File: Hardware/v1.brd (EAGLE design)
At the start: 50 x 40 mm, 83 parts, among them IC1 LM324D, IC2 m328p, IC3 REG1117, J2 22-27-2031-03, J3 22-27-2021-02, J4 22-27-2031-03, J5 22-27-2041-04, J6 22-27-2071-07, Q1 BSS123, Q2 BSS123, Q3 BSS123, Q5 BSS123

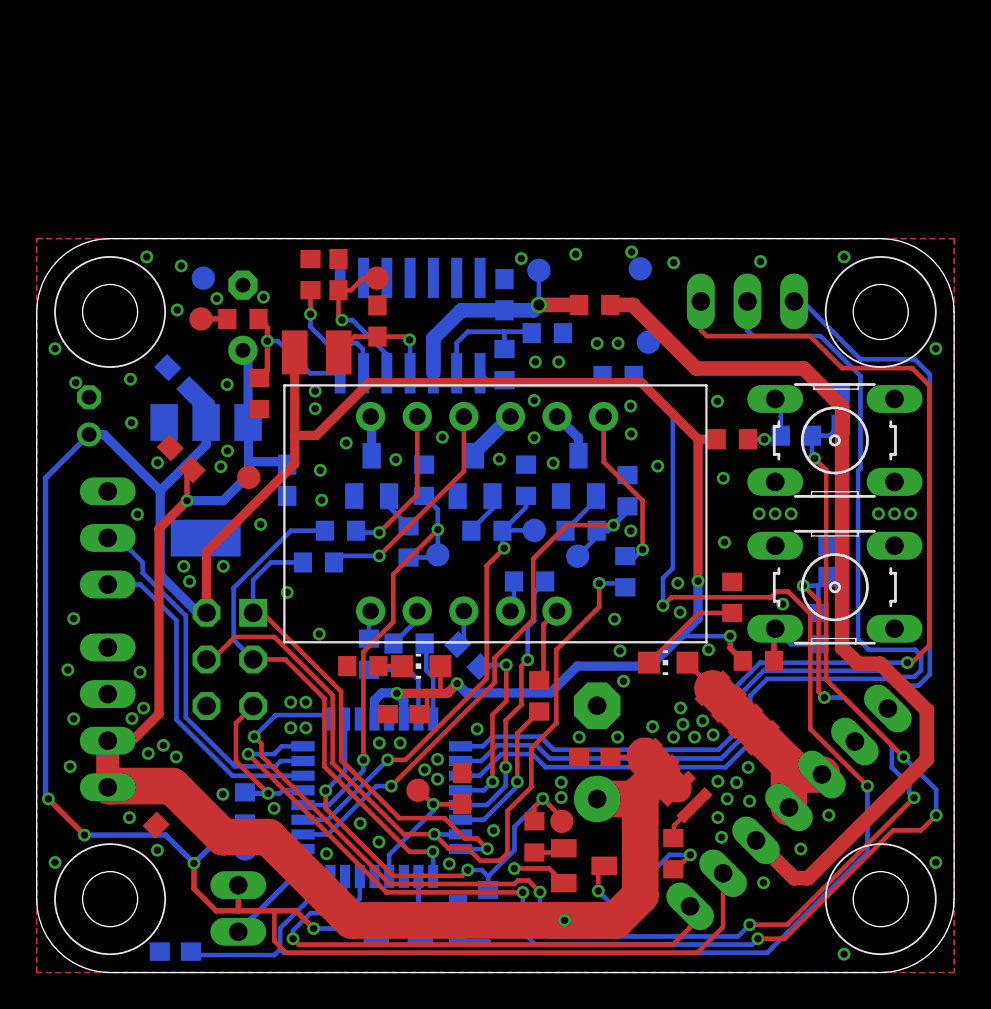
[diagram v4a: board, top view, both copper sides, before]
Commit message: all changes described in #64 pull ups are 10k
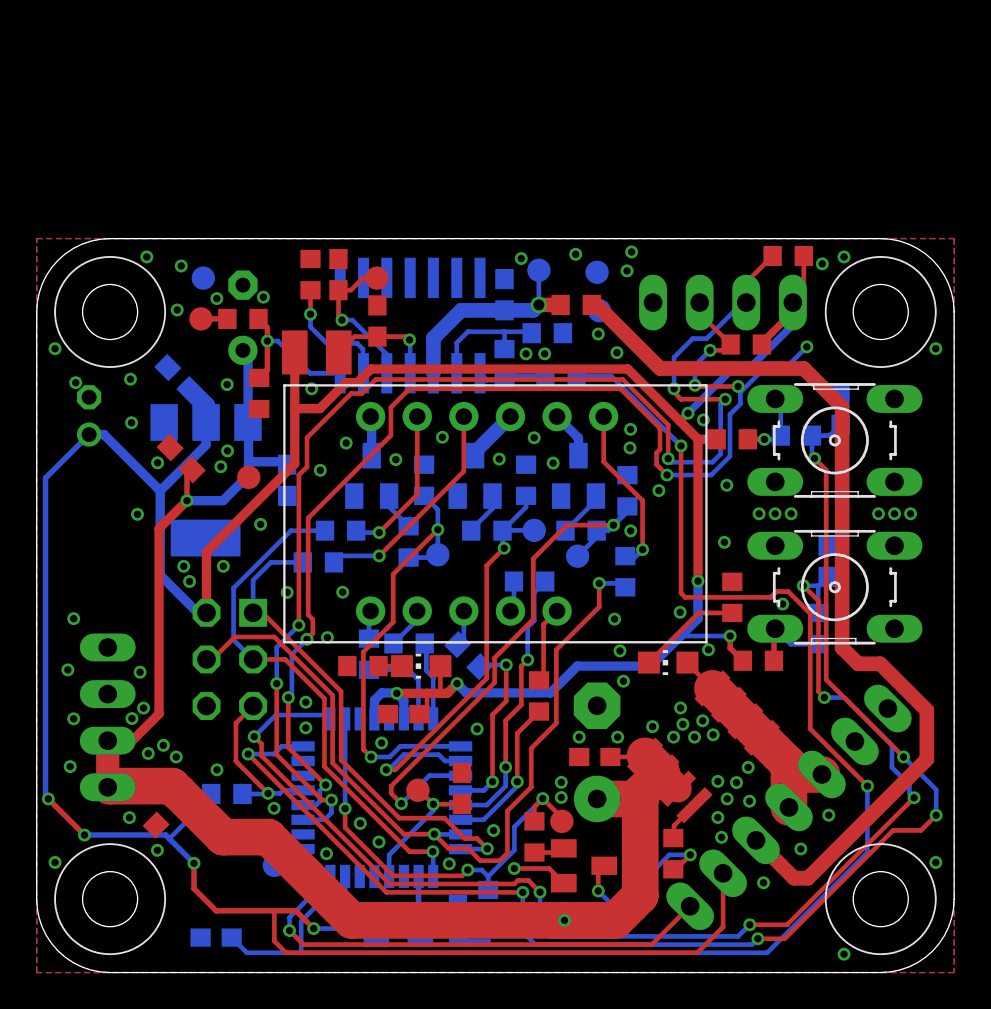
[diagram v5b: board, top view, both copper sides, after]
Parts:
- removed J2, J4: 22-27-2031-03, con-molex:6410-03
- removed J3: 22-27-2021-02, con-molex:6410-02
- added I2C: sda scl, con-molex:6410-04
- added R31, R32: 10k, rcl:R0603
- moved TP10 3.17 mm to (30.7, 36.1)
- moved R27 3.11 mm to (28.6, 32.5)
- moved TP9 2.36 mm to (30.5, 38.2)
- moved C16 2.35 mm to (9.78, 1.91)
- moved TP7 1.82 mm to (13.0, 5.84)
- moved R9 1.24 mm to (10.4, 9.73), turned to 180 degrees
- moved R30 1.02 mm to (29.4, 36.4)
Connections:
- removed net N$10: IC2.27, R20.2, R6.1, TP2.TP
- removed net N$2: IC2.26, R17.2, R5.1, TP3.TP
- removed net N$28: IC2.31, J2.2
- removed net N$29: IC2.30, J2.1
- removed net N$4: IC2.28, R21.2, R7.1, TP1.TP
- removed net PD5: IC2.9, J4.1
- removed net PD6: IC2.10, J4.2
- removed net PD7: IC2.11, J4.3
- removed net STH: IC2.24, J3.1
- new net DISP_FET_0: IC2.9, R21.2, R7.1, TP1.TP
- new net DISP_FET_1: IC2.10, R20.2, R6.1, TP2.TP
- new net DISP_FET_2: IC2.11, R17.2, R5.1, TP3.TP
- new net SCL: I2C.3, IC2.28, R32.1
- new net SDA: I2C.2, IC2.27, R31.1
- net GND: now also I2C.4; no longer J2.3
- net HALL: now also IC2.24; no longer IC2.22
- net VCC: now also I2C.1, R31.2, R32.2; no longer J3.2
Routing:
- net SDA: track 0.00 -> 67.6 mm, vias 0 -> 6
- net SCL: track 0.00 -> 66.3 mm, vias 0 -> 8
- net PD5: track 59.3 -> 0.00 mm, vias 1 -> 0
- net PD6: track 57.2 -> 0.00 mm
- net PD7: track 55.6 -> 0.00 mm
- net N$2: track 31.2 -> 0.00 mm, vias 2 -> 0
- net DISP_FET_2: track 0.00 -> 30.4 mm, vias 0 -> 2
- net N$10: track 25.8 -> 0.00 mm, vias 2 -> 0
- net DISP_FET_1: track 0.00 -> 24.7 mm, vias 0 -> 2
- net DISP_FET_0: track 0.00 -> 24.5 mm, vias 0 -> 2
- net N$4: track 24.1 -> 0.00 mm, vias 2 -> 0
- net N$28: track 19.5 -> 0.00 mm
- net N$29: track 18.1 -> 0.00 mm
- net VCC: track 179.5 -> 193.3 mm, vias 8 -> 9
- net STH: track 6.27 -> 0.00 mm
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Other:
- board text removed: "PD5"
- board text removed: "PD6"
- board text removed: "PD7"

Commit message: changed schematic (#65)
no real changes
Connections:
- net DISP_FET_0 renamed DISP_ENABLE_0
- net ENABLE_LED_0 renamed DISP_CC_0
- net ENABLE_LED_2 renamed DISP_CC_2
- new net DISP_CC_1: Q2.3
- new net DISP_ENABLE_1: R20.2, R6.1, TP2.TP
- new net DISP_ENABLE_2: R17.2, R5.1, TP3.TP
- net DISP_FET_1: no longer R20.2, R6.1, TP2.TP
- net DISP_FET_2: no longer R17.2, R5.1, TP3.TP
- net ENABLE_LED_1: no longer Q2.3
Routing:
- net DISP_FET_1: track 24.7 -> 19.7 mm
- net DISP_FET_2: track 30.4 -> 27.9 mm
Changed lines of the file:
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@@
 <signal name="ENABLE_LED_1">
 <contactref element="U$2" pad="P$4"/>
-<contactref element="Q2" pad="3"/>
-<wire x1="23.891875" y1="28.166875" x2="23.891875" y2="28.371875" width="0.254" layer="16"/>
 <wire x1="23.891875" y1="28.371875" x2="25.82" y2="30.3" width="0.762" layer="16"/>
 </signal>
-<signal name="ENABLE_LED_2">
+<signal name="DISP_CC_2">
 <contactref element="U$2" pad="P$5"/>
 <contactref element="Q1" pad="3"/>
@@
 <wire x1="29.5275" y1="29.1325" x2="28.36" y2="30.3" width="0.508" layer="16"/>
 </signal>
-<signal name="ENABLE_LED_0">
+<signal name="DISP_CC_0">
 <contactref element="U$2" pad="P$1"/>
 <contactref element="Q3" pad="3"/>
@@
 <wire x1="25.5905" y1="14.7955" x2="24.844375" y2="14.049375" width="0.254" layer="1"/>
 </signal>
-<signal name="DISP_FET_0">
+<signal name="DISP_ENABLE_0">
 <contactref element="R7" pad="1"/>
 <contactref element="TP1" pad="TP"/>
@@
 </signal>
 <signal name="DISP_FET_1">
-<contactref element="R6" pad="1"/>
-<contactref element="TP2" pad="TP"/>
-<contactref element="R20" pad="2"/>
 <wire x1="24.526875" y1="22.177375" x2="25.4762" y2="23.1267" width="0.254" layer="1"/>
 <via x="25.4762" y="23.1267" extent="1-16" drill="0.4"/>
-<wire x1="25.3864" y1="24.0792" x2="25.3864" y2="23.2165" width="0.254" layer="16"/>
 <wire x1="25.3864" y1="23.2165" x2="25.4762" y2="23.1267" width="0.254" layer="16"/>
-<wire x1="25.3864" y1="24.0792" x2="26.67" y2="25.3628" width="0.254" layer="16"/>
-<wire x1="26.67" y1="25.3628" x2="26.67" y2="25.97875" width="0.254" layer="16"/>
 <wire x1="19.542125" y1="11.049" x2="24.526875" y2="16.03375" width="0.254" layer="1"/>
 <wire x1="24.526875" y1="16.03375" x2="24.526875" y2="22.177375" width="0.254" layer="1"/>
-<wire x1="27.117675" y1="24.09825" x2="25.40545" y2="24.09825" width="0.254" layer="16"/>
-<wire x1="25.40545" y1="24.09825" x2="25.3864" y2="24.0792" width="0.254" layer="16"/>
 <contactref element="IC2" pad="10"/>
 <wire x1="19.542125" y1="11.049" x2="19.05" y2="11.049" width="0.254" layer="1"/>
@@
 </signal>
 <signal name="DISP_FET_2">
-<contactref element="R5" pad="1"/>
-<contactref element="TP3" pad="TP"/>
-<contactref element="R17" pad="2"/>
-<wire x1="30.5172" y1="24.0792" x2="30.5172" y2="24.11095" width="0.254" layer="16"/>
-<wire x1="30.5172" y1="24.0792" x2="30.362525" y2="24.0792" width="0.254" layer="16"/>
 <wire x1="24.9555" y1="17.145" x2="27.066875" y2="19.256375" width="0.254" layer="1"/>
 <wire x1="27.066875" y1="19.256375" x2="27.066875" y2="22.55625" width="0.254" layer="1"/>
@@
 <wire x1="31.15945" y1="24.11095" x2="31.4325" y2="24.384" width="0.3" layer="16"/>
 <wire x1="31.4325" y1="24.384" x2="32.1945" y2="25.146" width="0.3" layer="16"/>
-<wire x1="32.1945" y1="25.146" x2="32.1945" y2="25.40725" width="0.3" layer="16"/>
 <wire x1="27.066875" y1="22.55625" x2="28.894625" y2="24.384" width="0.254" layer="1"/>
 <wire x1="28.894625" y1="24.384" x2="31.4325" y2="24.384" width="0.254" layer="1"/>
 <via x="31.4325" y="24.384" extent="1-16" drill="0.4"/>
-<wire x1="30.5172" y1="23.852875" x2="30.5172" y2="24.0792" width="0.254" layer="16"/>
-<wire x1="29.48305" y1="22.691725" x2="30.5172" y2="23.725875" width="0.254" layer="16"/>
-<wire x1="30.5172" y1="23.725875" x2="30.5172" y2="24.0792" width="0.254" layer="16"/>
 <contactref element="IC2" pad="11"/>
 <wire x1="19.32305" y1="10.16" x2="19.32305" y2="9.75995" width="0.254" layer="1"/>
@@
 <wire x1="38.354" y1="31.8135" x2="38.354" y2="31.623" width="0.254" layer="16"/>
 </signal>
+<signal name="DISP_CC_1">
+<contactref element="Q2" pad="3"/>
+</signal>
+<signal name="DISP_ENABLE_1">
+<contactref element="R6" pad="1"/>
+<contactref element="TP2" pad="TP"/>
+<contactref element="R20" pad="2"/>
+<wire x1="27.117675" y1="24.09825" x2="26.67" y2="25.97875" width="0" layer="19" extent="16-16"/>
+<wire x1="25.3864" y1="24.0792" x2="27.117675" y2="24.09825" width="0" layer="19" extent="16-16"/>
+</signal>
+<signal name="DISP_ENABLE_2">
+<contactref element="R17" pad="2"/>
+<contactref element="R5" pad="1"/>
+<contactref element="TP3" pad="TP"/>
+<wire x1="30.5172" y1="24.0792" x2="32.1945" y2="25.40725" width="0" layer="19" extent="16-16"/>
+<wire x1="29.48305" y1="22.691725" x2="30.5172" y2="24.0792" width="0" layer="19" extent="16-16"/>
+</signal>
 </signals>

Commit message: something .. i dont know ?!
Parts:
- removed TP11, TP12, TP7: PTR1B1,27, testpad:B1,27
- added D4: (no value), diode:DO214AC
- added J1: UART, con-molex:6410-03
- added Q4: BSS123, transistor-small-signal:SOT23
- added R33: 330k, rcl:R0603
- added R34: 20k, rcl:R0603
- added R35, R38, R42: 100k, rcl:R0603
- added R39: 68k, rcl:R0603
- added R40: 220k, rcl:R0603
- added R41: 200k, rcl:R0603
- added R43: 11k, rcl:R0603
- added R44: 6.2k, rcl:R0603
- C10: value n.m. -> 1u; device rcl:C0603 -> rcl:C0805
- IC1: value LM324D -> TS914I
- R1: value 43k -> 430k
- R16, R2: value 100 -> 1k
- R24: value n.m. -> 10k
- R25: value n.m. -> 100
- R28: value n.m. -> 1k
- moved C16 38.2 mm to (32.4, 32.6), turned to 180 degrees
- moved R24 24.3 mm to (34.5, 41.1), turned to 270 degrees
- moved R25 18.2 mm to (32.9, 41.1)
- moved C10 13.2 mm to (28.0, 44.5), turned to 0 degrees
- moved R28 9.97 mm to (18.4, 42.5)
- moved R19 0.13 mm to (38.0, 29.1)
- moved R16 0.06 mm to (27.1, 7.33)
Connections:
- net SDFGHJK renamed THERMO0_RAW
- removed net DISP_FET_1: IC2.10
- removed net DISP_FET_2: IC2.11
- removed net ENABLE_LED_1: U$2.P$4
- removed net N$30: C10.1, IC1.5, TP11.TP
- new net ADC3: IC2.26
- new net N$10: Q4.1, R24.1, R25.1
- new net N$2: IC2.31, J1.3
- new net N$28: R42.1, R43.1, R44.2
- new net N$29: IC1.14, R25.2, R41.2
- new net N$4: IC2.30, J1.2
- new net SAFETY: Q4.3, Q5.1, R16.1
- new net THERMO_COARSE: IC1.7, R33.2, R34.1
- new net THERMO_COARSE_INV: D4.A, IC1.8, R35.2
- new net THERMO_VOLTAGE: C10.1, D4.C, IC1.13, R40.2
- net ADC2: no longer TP7.TP
- net DISP_CC_1: now also U$2.P$4
- net DISP_ENABLE_1: now also IC2.10
- net DISP_ENABLE_2: now also IC2.11
- net GND: now also J1.1, Q4.2, R24.2, R28.2, R38.2, R40.1, R44.1; no longer R24.1, R25.1
- net N$16: now also IC1.6, R28.1, R33.1; no longer Q5.1, R16.1
- net N$20: now also IC1.9, R34.2, R35.1; no longer IC1.6, R25.2
- net N$21: now also IC1.12, R41.1, R42.2; no longer R28.1, TP12.TP
- net N$26: now also IC1.10, R38.1, R39.2; no longer IC1.7, R24.2, R28.2
- net SENSOR0: now also IC1.5
- net VCC: now also R39.1, R43.2
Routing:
- net SAFETY: track 0.00 -> 56.4 mm, vias 0 -> 2
- net ADC2: track 1.93 -> 38.5 mm, vias 0 -> 1
- net DISP_ENABLE_2: track 0.00 -> 29.7 mm, vias 0 -> 2
- net DISP_FET_2: track 27.9 -> 0.00 mm, vias 2 -> 0
- net LOETKOLBEN_0: track 24.4 -> 50.2 mm, vias 3 -> 6
- net DISP_ENABLE_1: track 0.00 -> 24.3 mm, vias 0 -> 2
- net N$2: track 0.00 -> 21.9 mm, vias 0 -> 1
- net N$4: track 0.00 -> 21.5 mm
- net DISP_FET_1: track 19.7 -> 0.00 mm, vias 2 -> 0
- net THERMO0_RAW: track 3.82 -> 13.3 mm, vias 0 -> 1
- net N$30: track 8.36 -> 0.00 mm, vias 1 -> 0
- net N$26: track 8.30 -> 0.00 mm, vias 1 -> 0
- net N$20: track 6.69 -> 0.00 mm, vias 1 -> 0
- net THERMO0: track 80.9 -> 76.7 mm
- net N$10: track 0.00 -> 3.45 mm
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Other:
- board size 50 x 40 mm -> 50 x 50 mm
- board text removed: "PD0"
- board text removed: "PD1"
